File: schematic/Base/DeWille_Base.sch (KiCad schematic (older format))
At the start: 4 parts, among them J101 HN2x10, J102 HN2x10, J103 HN2x10

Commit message: Base schematic complete
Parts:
- removed J101, J102, J103: HN2x10, Connector_PinHeader_2.54mm:PinHeader_2x10_P2.54mm_Vertical, symbol Connector_Generic:Conn_02x10_Odd_Even
- removed L101: 100 Ohm@100MHz, Inductor_SMD:L_0805_2012Metric, symbol Device:L_Core_Ferrite
- added B101: DeWille_Control, Zmei_Footprints:DeWille_Control, symbol Zmei_elements:DeWille_Control
- added B102, B103: DeWille_DAC, Zmei_Footprints:DeWille_DAC, symbol Zmei_elements:DeWille_DAC
- added B104, B105: DeWille_ItoV, Zmei_Footprints:DeWille_ItoV, symbol Zmei_elements:DeWille_ItoV
- added J101: Out Left, TerminalBlock_Dinkle:TerminalBlock_Dinkle_DT-55-B01X-03_P10.00mm, symbol Connector_Generic:Conn_01x03
- added J102: Out Right, TerminalBlock_Dinkle:TerminalBlock_Dinkle_DT-55-B01X-03_P10.00mm, symbol Connector_Generic:Conn_01x03
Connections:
- net labels added: MISOL, MISOR, MOSIL, MOSIR, SCLKL, SCLKR
- net labels removed: +5V, BCK, BCK2, DATA1, DATA2, LRCK1, LRCK2, MISO, MOSI, SCK1, SCK2, SCLK, SPDIF1, SPDIF2
- wire segments 91 -> 136
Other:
- note added: "+3V3_ISOL referenced against GNDD!"
- note removed: "Control"

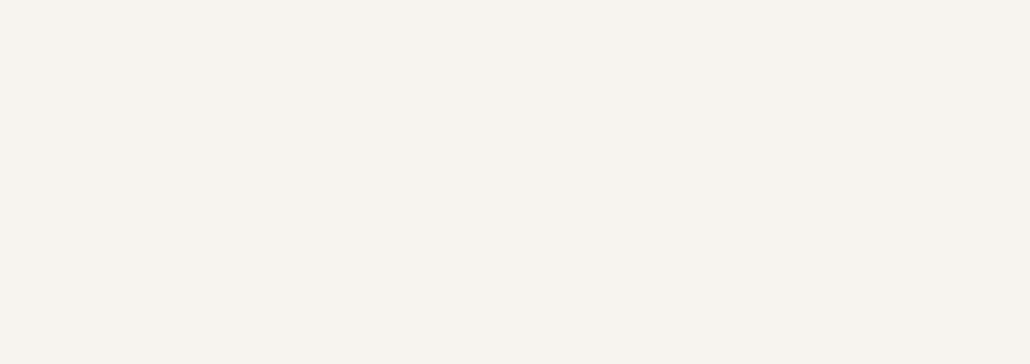
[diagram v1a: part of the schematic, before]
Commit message: Add Changes.txt, listing future changes to the schematic and boards Finish up Base board routing
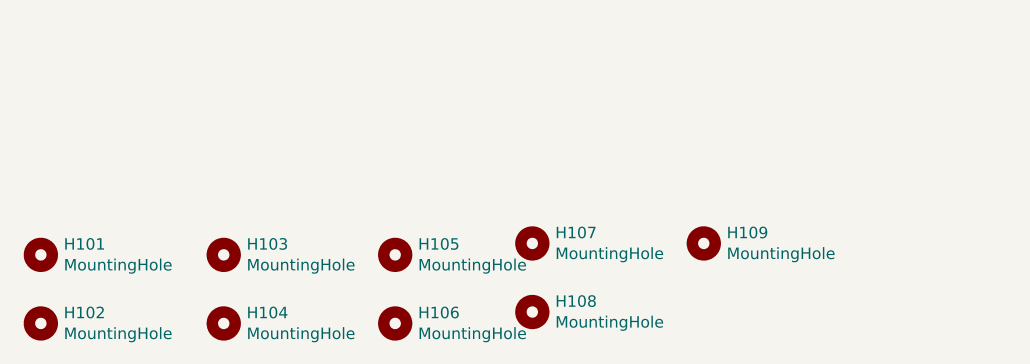
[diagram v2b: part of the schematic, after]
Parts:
- added H101, H102, H103, H104, H105, H106, H107, H108, H109: MountingHole, MountingHole:MountingHole_3.2mm_M3_Pad, symbol Mechanical:MountingHole
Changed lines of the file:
@@
 	9350 6900 9350 7100
 Connection ~ 9250 7000
+$Comp
+L Mechanical:MountingHole H102
+U 1 1 5E150DBB
+P 2300 10500
+F 0 "H102" H 2400 10546 50  0000 L CNN
+F 1 "MountingHole" H 2400 10455 50  0000 L CNN
+F 2 "MountingHole:MountingHole_3.2mm_M3_Pad" H 2300 10500 50  0001 C CNN
+F 3 "~" H 2300 10500 50  0001 C CNN
+	1    2300 10500
+	1    0    0    -1
+$EndComp
+$Comp
+L Mechanical:MountingHole H101
+U 1 1 5E15181F
+P 2300 10200
+F 0 "H101" H 2400 10246 50  0000 L CNN
+F 1 "MountingHole" H 2400 10155 50  0000 L CNN
+F 2 "MountingHole:MountingHole_3.2mm_M3_Pad" H 2300 10200 50  0001 C CNN
+F 3 "~" H 2300 10200 50  0001 C CNN
+	1    2300 10200
+	1    0    0    -1
+$EndComp
+$Comp
+L Mechanical:MountingHole H103
+U 1 1 5E151E05
+P 3100 10200
+F 0 "H103" H 3200 10246 50  0000 L CNN
+F 1 "MountingHole" H 3200 10155 50  0000 L CNN
+F 2 "MountingHole:MountingHole_3.2mm_M3_Pad" H 3100 10200 50  0001 C CNN
+F 3 "~" H 3100 10200 50  0001 C CNN
+	1    3100 10200
+	1    0    0    -1
+$EndComp
+$Comp
+L Mechanical:MountingHole H104
+U 1 1 5E15203C
+P 3100 10500
+F 0 "H104" H 3200 10546 50  0000 L CNN
+F 1 "MountingHole" H 3200 10455 50  0000 L CNN
+F 2 "MountingHole:MountingHole_3.2mm_M3_Pad" H 3100 10500 50  0001 C CNN
+F 3 "~" H 3100 10500 50  0001 C CNN
+	1    3100 10500
+	1    0    0    -1
+$EndComp
+$Comp
+L Mechanical:MountingHole H105
+U 1 1 5E15241C
+P 3850 10200
+F 0 "H105" H 3950 10246 50  0000 L CNN
+F 1 "MountingHole" H 3950 10155 50  0000 L CNN
+F 2 "MountingHole:MountingHole_3.2mm_M3_Pad" H 3850 10200 50  0001 C CNN
+F 3 "~" H 3850 10200 50  0001 C CNN
+	1    3850 10200
+	1    0    0    -1
+$EndComp
+$Comp
+L Mechanical:MountingHole H106
+U 1 1 5E1527A7
+P 3850 10500
+F 0 "H106" H 3950 10546 50  0000 L CNN
+F 1 "MountingHole" H 3950 10455 50  0000 L CNN
+F 2 "MountingHole:MountingHole_3.2mm_M3_Pad" H 3850 10500 50  0001 C CNN
+F 3 "~" H 3850 10500 50  0001 C CNN
+	1    3850 10500
+	1    0    0    -1
+$EndComp
+$Comp
+L Mechanical:MountingHole H107
+U 1 1 5E152AFF
+P 4450 10150
+F 0 "H107" H 4550 10196 50  0000 L CNN
+F 1 "MountingHole" H 4550 10105 50  0000 L CNN
+F 2 "MountingHole:MountingHole_3.2mm_M3_Pad" H 4450 10150 50  0001 C CNN
+F 3 "~" H 4450 10150 50  0001 C CNN
+	1    4450 10150
+	1    0    0    -1
+$EndComp
+$Comp
+L Mechanical:MountingHole H108
+U 1 1 5E152E9B
+P 4450 10450
+F 0 "H108" H 4550 10496 50  0000 L CNN
+F 1 "MountingHole" H 4550 10405 50  0000 L CNN
+F 2 "MountingHole:MountingHole_3.2mm_M3_Pad" H 4450 10450 50  0001 C CNN
+F 3 "~" H 4450 10450 50  0001 C CNN
+	1    4450 10450
+	1    0    0    -1
+$EndComp
+$Comp
+L Mechanical:MountingHole H109
+U 1 1 5E6AD862
+P 5200 10150
+F 0 "H109" H 5300 10196 50  0000 L CNN
+F 1 "MountingHole" H 5300 10105 50  0000 L CNN
+F 2 "MountingHole:MountingHole_3.2mm_M3_Pad" H 5200 10150 50  0001 C CNN
+F 3 "~" H 5200 10150 50  0001 C CNN
+	1    5200 10150
+	1    0    0    -1
+$EndComp
 $EndSCHEMATC
